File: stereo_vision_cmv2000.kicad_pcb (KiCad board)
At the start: 4 copper layers, 40 parts, among them P101 FI-RE51S-HF-R1500, U201 AP1084, U202 MCP1826S, U203 NCP1117ST20T3G, U401 CMV2000

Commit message: basic routing done
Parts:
- removed C218, C222, C228, C230, C407: 100n, SMD_Packages:SM0402_c
- removed TP401, TP402, TP403: TESTPOINT, Connect:TESTPOINT
- added C101: 100µ, SMD_Packages:SM1210, B.Cu at (117.7, 117.7)
- added C102: 100µ, SMD_Packages:SM1210, B.Cu at (117.7, 121.3)
- added C103: 100µ, SMD_Packages:SM1210, B.Cu at (117.7, 114.2)
- added C201: 100µ, SMD_Packages:SM1210, F.Cu at (154.1, 102.4)
- added C202: 100µ, SMD_Packages:SM1210, B.Cu at (147.6, 110.1)
- added C203: 330µ, Capacitors_SMD:c_elec_6.3x7.7, F.Cu at (153.4, 108.0)
- added C204: 33µ, SMD_Packages:SM0603_Capa, B.Cu at (147.3, 118.1)
- added C205: 10µ, SMD_Packages:SM0603_Capa, B.Cu at (148.1, 107.6)
- added C206: 10µ, SMD_Packages:SM0603_Capa, B.Cu at (147.3, 115.1)
- added C207: 330µ, Capacitors_SMD:c_elec_6.3x7.7, F.Cu at (153.4, 115.8)
- added C209: 10µ, SMD_Packages:SM0603_Capa, F.Cu at (153.8, 100.0)
- added C211: 330µ, Capacitors_SMD:c_elec_6.3x7.7, F.Cu at (153.4, 123.8)
- added C301: 4.7µ, SMD_Packages:SM0402_c, B.Cu at (138.2, 121.5)
- added C302: 100n, SMD_Packages:SM0402_c, B.Cu at (139.8, 116.5)
- added C306: 100n, SMD_Packages:SM0402_c, B.Cu at (131.8, 110.1)
- added C309: 4.7µ, SMD_Packages:SM0402_c, B.Cu at (121.5, 117.7)
- added C310: 4.7µ, SMD_Packages:SM0402_c, B.Cu at (139.8, 115.7)
- added C313: 4.7µ, SMD_Packages:SM0402_c, B.Cu at (129.6, 110.1)
- added C314: 4.7µ, SMD_Packages:SM0402_c, B.Cu at (121.5, 113.4)
- added C317: 4.7µ, SMD_Packages:SM0402_c, B.Cu at (131.1, 121.5)
- added C319: 4.7µ, SMD_Packages:SM0402_c, B.Cu at (121.5, 118.5)
- added C331: 100n, SMD_Packages:SM0402_c, B.Cu at (121.5, 116.2)
- added D201: LED, LEDs:LED-0603, F.Cu at (147.3, 103.0)
- added R201: 680, SMD_Packages:SM0603, F.Cu at (148.8, 103.0)
- added R302: R, SMD_Packages:SM0603, F.Cu at (139.3, 97.6)
- added R303: R, SMD_Packages:SM0603, F.Cu at (142.3, 97.6)
- added R304: 10k, SMD_Packages:SM0603, F.Cu at (143.8, 97.6)
- added R305: R, SMD_Packages:SM0603, F.Cu at (140.8, 97.6)
- added SYM: Symbol_OSHW-Logo_SilkScreen_07Jul2012, Symbols:Symbol_OSHW-Logo_SilkScreen, F.Cu at (112.3, 102.1)
- added TP301: TESTPOINT, Measurement_Points:Measurement_Point_Round-SMD-Pad_Small, F.Cu at (149.7, 129.3)
- added TP302: TESTPOINT, Measurement_Points:Measurement_Point_Round-SMD-Pad_Small, F.Cu at (151.8, 129.3)
- added TP303: TESTPOINT, Measurement_Points:Measurement_Point_Round-SMD-Pad_Small, F.Cu at (147.7, 129.3)
- added U401: MOUNTHOLE, owncomp:MOUNTING_HOLE, F.Cu at (110.8, 130.6)
- added U402: MOUNTHOLE, owncomp:MOUNTING_HOLE, F.Cu at (110.8, 95.6)
- added U403: MOUNTHOLE, owncomp:MOUNTING_HOLE, F.Cu at (155.8, 95.6)
- added U404: MOUNTHOLE, owncomp:MOUNTING_HOLE, F.Cu at (155.8, 130.6)
- added U405: MOUNTHOLE, owncomp:MOUNTING_HOLE, F.Cu at (142.8, 128.1)
- added U407: MOUNTHOLE, owncomp:MOUNTING_HOLE, F.Cu at (118.8, 104.1)
- added U408: MOUNTHOLE, owncomp:MOUNTING_HOLE, F.Cu at (118.8, 128.1)
- C208, C212: value 100n -> 33µ; footprint SMD_Packages:SM0402_c -> SMD_Packages:SM0603_Capa; moved to B.Cu
- C210: value 100n -> 10µ; footprint SMD_Packages:SM0402_c -> SMD_Packages:SM0603_Capa; moved to B.Cu
- C308: renamed from C214; moved to B.Cu
- C312: renamed from C217; moved to B.Cu
- C316: renamed from C221; moved to B.Cu
- C318: renamed from C224; moved to B.Cu
- C320: renamed from C226; moved to B.Cu
- C325: renamed from C401; moved to B.Cu
- C326: renamed from C402; moved to B.Cu
- C327: renamed from C403; moved to B.Cu
- C328: renamed from C404; moved to B.Cu
- C329: renamed from C405; moved to B.Cu
- C330: renamed from C406; moved to B.Cu
- C332: renamed from C408; moved to B.Cu
- C333: renamed from C409; moved to B.Cu
- C334: renamed from C410; moved to B.Cu
- C335: renamed from C411; moved to B.Cu
- C336: renamed from C412; moved to B.Cu
- C337: renamed from C413; moved to B.Cu
- C338: renamed from C414; moved to B.Cu
- C339: renamed from C415; moved to B.Cu
- C340: renamed from C416; moved to B.Cu
- C341: renamed from C417; moved to B.Cu
- C342: renamed from C418; moved to B.Cu
- C343: renamed from C419; moved to B.Cu
- P101: moved to B.Cu
- R301: renamed from R201; moved to B.Cu
- U201: value AP1084 -> 3.3V; moved to B.Cu
- U202: value MCP1826S -> 3.0V; moved to B.Cu
- U203: value NCP1117ST20T3G -> 2.0V; moved to B.Cu
- U301: renamed from U401; value CMV2000 -> CMV2000/4000
- moved C338 85.9 mm to (123.8, 121.5)
- moved U203 55.8 mm to (153.6, 123.8)
- moved U202 43.6 mm to (153.6, 115.8), turned to 90 degrees
- moved U201 41.8 mm to (154.1, 108.1), turned to 0 degrees
- moved C320 29.3 mm to (121.5, 119.3)
- moved C334 28.3 mm to (124.6, 121.5), turned to 90 degrees
- moved C336 28.1 mm to (125.3, 121.5), turned to 90 degrees
- moved C337 26.5 mm to (121.5, 114.9)
- moved C329 26.4 mm to (121.5, 112.6)
- moved C325 25.8 mm to (126.9, 121.5), turned to 90 degrees
- moved C312 25.8 mm to (121.5, 114.2)
- moved C308 25.7 mm to (121.5, 117.0)
- moved C326 24.1 mm to (126.9, 123.6), turned to 270 degrees
- moved C335 23.0 mm to (127.6, 121.5), turned to 90 degrees
- moved C343 23.0 mm to (126.1, 121.5), turned to 90 degrees
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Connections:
- net /OMV2000/LVDS_9_N renamed /CMV2000/LVDS_9_N
- net /OMV2000/LVDS_9_P renamed /CMV2000/LVDS_9_P
- net /OMV2000/SPI_CLK renamed /CMV2000/SPI_CLK
- net /OMV2000/SPI_IN renamed /CMV2000/SPI_IN
- net /OMV2000/SPI_OUT renamed /CMV2000/SPI_OUT
- C208 pad 1: GND -> /CMV2000/3.0V
- C208 pad 2: /OMV2000/3.3V -> GND
- C210 pad 1: GND -> /CMV2000/2.0V
- C210 pad 2: /OMV2000/2.0V -> GND
- C212 pad 1: GND -> /CMV2000/2.0V
- C212 pad 2: /OMV2000/2.0V -> GND
- C308 pad 2: /OMV2000/2.0V -> /CMV2000/2.0V
- C312 pad 2: /OMV2000/3.3V -> /CMV2000/3.3V
- C316 pad 2: /OMV2000/3.3V -> /CMV2000/3.3V
- C318 pad 2: /OMV2000/3.3V -> /CMV2000/3.3V
- C320 pad 2: /OMV2000/3.0V -> /CMV2000/3.0V
- C325 pad 1: /OMV2000/3.3V -> /CMV2000/3.3V
- C326 pad 1: /OMV2000/3.3V -> /CMV2000/3.3V
- C327 pad 1: /OMV2000/3.3V -> /CMV2000/3.3V
- C328 pad 1: /OMV2000/3.3V -> /CMV2000/3.3V
- P101 pad 1: /OMV2000/LVDS_1_N -> /CMV2000/LVDS_CLK_OUT_N
- P101 pad 10: /OMV2000/LVDS_5_P -> /CMV2000/LVDS_14_P
- P101 pad 11: /OMV2000/LVDS_6_P -> /CMV2000/LVDS_12_N
- P101 pad 12: /OMV2000/LVDS_6_N -> /CMV2000/LVDS_12_P
- P101 pad 13: /OMV2000/LVDS_7_N -> /CMV2000/LVDS_11_N
- P101 pad 14: /OMV2000/LVDS_7_P -> /CMV2000/LVDS_11_P
- P101 pad 15: /OMV2000/LVDS_8_N -> /CMV2000/LVDS_10_N
- P101 pad 16: /OMV2000/LVDS_8_P -> /CMV2000/LVDS_10_P
- P101 pad 19: /OMV2000/LVDS_10_N -> /CMV2000/LVDS_7_N
- P101 pad 2: /OMV2000/LVDS_1_P -> /CMV2000/LVDS_CLK_OUT_P
- P101 pad 20: /OMV2000/LVDS_10_P -> /CMV2000/LVDS_7_P
- P101 pad 21: /OMV2000/LVDS_11_N -> /CMV2000/LVDS_8_N
- P101 pad 22: /OMV2000/LVDS_11_P -> /CMV2000/LVDS_8_P
- P101 pad 23: /OMV2000/LVDS_12_N -> /CMV2000/LVDS_5_N
- P101 pad 24: /OMV2000/LVDS_12_P -> /CMV2000/LVDS_5_P
- P101 pad 25: /OMV2000/LVDS_13_N -> /CMV2000/LVDS_6_N
- P101 pad 26: /OMV2000/LVDS_13_P -> /CMV2000/LVDS_6_P
- P101 pad 27: /OMV2000/LVDS_14_P -> /CMV2000/LVDS_4_N
- P101 pad 28: /OMV2000/LVDS_14_N -> /CMV2000/LVDS_4_P
- P101 pad 29: /OMV2000/LVDS_15_N -> /CMV2000/LVDS_3_N
- P101 pad 3: /OMV2000/LVDS_2_N -> /CMV2000/LVDS_15_N
- P101 pad 30: /OMV2000/LVDS_15_P -> /CMV2000/LVDS_3_P
- P101 pad 31: /OMV2000/LVDS_16_N -> /CMV2000/LVDS_2_N
- P101 pad 32: /OMV2000/LVDS_16_P -> /CMV2000/LVDS_2_P
- P101 pad 33: /OMV2000/LVDS_CTR_N -> /CMV2000/LVDS_1_N
- P101 pad 34: /OMV2000/LVDS_CTR_P -> /CMV2000/LVDS_1_P
- P101 pad 35: /OMV2000/LVDS_CLK_OUT_N -> /CMV2000/LVDS_CTR_N
- P101 pad 36: /OMV2000/LVDS_CLK_OUT_P -> /CMV2000/LVDS_CTR_P
- P101 pad 37: Net-(P101-Pad37) -> /CMV2000/LVDS_CLK_IN_N
- P101 pad 38: /OMV2000/FRAME_REQ -> /CMV2000/LVDS_CLK_IN_P
- P101 pad 39: /OMV2000/T_EXP1 -> /CMV2000/FRAME_REQ
- P101 pad 4: /OMV2000/LVDS_2_P -> /CMV2000/LVDS_15_P
- P101 pad 40: /OMV2000/T_EXP2 -> /CMV2000/CLK_IN
- P101 pad 41: /OMV2000/SYS_RES_N -> /CMV2000/T_EXP2
- P101 pad 44: /OMV2000/SPI_EN -> /CMV2000/T_EXP1
- P101 pad 46: Net-(P101-Pad46) -> /CMV2000/SPI_EN
- P101 pad 47: Net-(P101-Pad47) -> /CMV2000/SYS_RES_N
- P101 pad 48: Net-(P101-Pad48) -> /Power Supply/5V
- P101 pad 49: Net-(P101-Pad49) -> /Power Supply/5V
- P101 pad 5: /OMV2000/LVDS_3_N -> /CMV2000/LVDS_16_N
- P101 pad 50: /OMV2000/LVDS_CLK_IN_N -> GND
- P101 pad 51: /OMV2000/LVDS_CLK_IN_P -> GND
- P101 pad 52: Net-(P101-Pad52) -> GND
- P101 pad 53: Net-(P101-Pad53) -> GND
- P101 pad 54: Net-(P101-Pad54) -> GND
- P101 pad 55: Net-(P101-Pad55) -> GND
- P101 pad 56: Net-(P101-Pad56) -> GND
- P101 pad 57: Net-(P101-Pad57) -> GND
- P101 pad 58: Net-(P101-Pad58) -> GND
- P101 pad 59: Net-(P101-Pad59) -> GND
- P101 pad 6: /OMV2000/LVDS_3_P -> /CMV2000/LVDS_16_P
- P101 pad 60: Net-(P101-Pad60) -> GND
- P101 pad 61: Net-(P101-Pad61) -> GND
- P101 pad 7: /OMV2000/LVDS_4_N -> /CMV2000/LVDS_13_N
- P101 pad 8: /OMV2000/LVDS_4_P -> /CMV2000/LVDS_13_P
- P101 pad 9: /OMV2000/LVDS_5_N -> /CMV2000/LVDS_14_N
- R301 pad 1: /OMV2000/LVDS_CLK_IN_N -> /CMV2000/LVDS_CLK_IN_N
- R301 pad 2: /OMV2000/LVDS_CLK_IN_P -> /CMV2000/LVDS_CLK_IN_P
- U201 pad 2: /OMV2000/3.3V -> /CMV2000/3.3V
- U202 pad 1: /OMV2000/3.3V -> /CMV2000/3.3V
- U202 pad 3: /OMV2000/3.0V -> /CMV2000/3.0V
- U203 pad 2: /OMV2000/2.0V -> /CMV2000/2.0V
- U203 pad 4: (no net) -> /CMV2000/2.0V
- U301 pad A10: /OMV2000/LVDS_15_N -> /CMV2000/LVDS_15_N
- U301 pad A11: /OMV2000/LVDS_15_P -> /CMV2000/LVDS_15_P
- U301 pad A2: /OMV2000/LVDS_2_N -> /CMV2000/LVDS_2_N
- U301 pad A3: /OMV2000/LVDS_2_P -> /CMV2000/LVDS_2_P
- U301 pad A4: /OMV2000/LVDS_5_N -> /CMV2000/LVDS_5_N
- U301 pad A5: /OMV2000/LVDS_5_P -> /CMV2000/LVDS_5_P
- U301 pad A7: /OMV2000/2.0V -> /CMV2000/2.0V
- U301 pad A8: /OMV2000/LVDS_12_N -> /CMV2000/LVDS_12_N
- U301 pad A9: /OMV2000/LVDS_12_P -> /CMV2000/LVDS_12_P
- U301 pad B1: /OMV2000/LVDS_CTR_N -> /CMV2000/LVDS_CTR_N
- U301 pad B10: /OMV2000/LVDS_13_P -> /CMV2000/LVDS_13_P
- U301 pad B11: /OMV2000/LVDS_CLK_OUT_N -> /CMV2000/LVDS_CLK_OUT_N
- U301 pad B12: /OMV2000/LVDS_CLK_OUT_P -> /CMV2000/LVDS_CLK_OUT_P
- U301 pad B2: /OMV2000/LVDS_CTR_P -> /CMV2000/LVDS_CTR_P
- U301 pad B3: /OMV2000/LVDS_4_N -> /CMV2000/LVDS_4_N
- U301 pad B4: /OMV2000/LVDS_4_P -> /CMV2000/LVDS_4_P
- U301 pad B5: /OMV2000/LVDS_7_N -> /CMV2000/LVDS_7_N
- U301 pad B6: /OMV2000/LVDS_7_P -> /CMV2000/LVDS_7_P
- U301 pad B7: /OMV2000/LVDS_10_N -> /CMV2000/LVDS_10_N
- U301 pad B8: /OMV2000/LVDS_10_P -> /CMV2000/LVDS_10_P
- U301 pad B9: /OMV2000/LVDS_13_N -> /CMV2000/LVDS_13_N
- U301 pad C10: /OMV2000/LVDS_16_N -> /CMV2000/LVDS_16_N
- U301 pad C11: /OMV2000/LVDS_16_P -> /CMV2000/LVDS_16_P
- U301 pad C2: /OMV2000/LVDS_1_N -> /CMV2000/LVDS_1_N
- U301 pad C3: /OMV2000/LVDS_1_P -> /CMV2000/LVDS_1_P
- U301 pad C4: /OMV2000/LVDS_6_N -> /CMV2000/LVDS_6_N
- U301 pad C5: /OMV2000/LVDS_6_P -> /CMV2000/LVDS_6_P
- U301 pad C7: /OMV2000/2.0V -> /CMV2000/2.0V
- U301 pad C8: /OMV2000/LVDS_11_N -> /CMV2000/LVDS_11_N
- U301 pad C9: /OMV2000/LVDS_11_P -> /CMV2000/LVDS_11_P
- U301 pad D1: /OMV2000/LVDS_CLK_IN_P -> /CMV2000/LVDS_CLK_IN_P
- U301 pad D10: /OMV2000/LVDS_14_P -> /CMV2000/LVDS_14_P
- U301 pad D2: /OMV2000/LVDS_CLK_IN_N -> /CMV2000/LVDS_CLK_IN_N
- U301 pad D3: /OMV2000/LVDS_3_N -> /CMV2000/LVDS_3_N
- U301 pad D4: /OMV2000/LVDS_3_P -> /CMV2000/LVDS_3_P
- U301 pad D5: /OMV2000/LVDS_8_N -> /CMV2000/LVDS_8_N
- U301 pad D6: /OMV2000/LVDS_8_P -> /CMV2000/LVDS_8_P
- U301 pad D9: /OMV2000/LVDS_14_N -> /CMV2000/LVDS_14_N
- U301 pad E1: /OMV2000/CLK_IN -> /CMV2000/CLK_IN
- U301 pad E2: /OMV2000/3.3V -> /CMV2000/3.3V
- U301 pad E4: /OMV2000/2.0V -> /CMV2000/2.0V
- U301 pad E6: /OMV2000/3.0V -> /CMV2000/3.0V
- U301 pad E7: /OMV2000/2.0V -> /CMV2000/2.0V
- U301 pad E8: /OMV2000/2.0V -> /CMV2000/2.0V
- U301 pad F2: /OMV2000/FRAME_REQ -> /CMV2000/FRAME_REQ
- U301 pad F7: /OMV2000/3.3V -> /CMV2000/3.3V
- U301 pad G1: /OMV2000/3.0V -> /CMV2000/3.0V
- U301 pad G12: /OMV2000/3.0V -> /CMV2000/3.0V
- U301 pad G3: /OMV2000/T_EXP2 -> /CMV2000/T_EXP2
- U301 pad G4: /OMV2000/SPI_EN -> /CMV2000/SPI_EN
- U301 pad H1: /OMV2000/3.3V -> /CMV2000/3.3V
- U301 pad H3: /OMV2000/T_EXP1 -> /CMV2000/T_EXP1
- U301 pad H5: /OMV2000/SYS_RES_N -> /CMV2000/SYS_RES_N
- U301 pad H6: /OMV2000/3.3V -> /CMV2000/3.3V
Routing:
- net /CMV2000/3.3V: track 0.00 -> 136.4 mm, vias 0 -> 25
- net /CMV2000/2.0V: track 0.00 -> 85.1 mm, vias 0 -> 18
- net (no net): track 0.00 -> 71.1 mm, vias 0 -> 54
- net GND: track 34.3 -> 105.4 mm, vias 0 -> 37
- net /CMV2000/3.0V: track 0.00 -> 58.7 mm, vias 0 -> 16
- net /Power Supply/5V: track 0.00 -> 51.8 mm, vias 0 -> 15
- net /OMV2000/3.3V: track 48.2 -> 0.00 mm, vias 12 -> 0
- net /CMV2000/SYS_RES_N: track 0.00 -> 37.0 mm, vias 0 -> 1
- net /CMV2000/SPI_EN: track 0.00 -> 31.2 mm, vias 0 -> 1
- net /CMV2000/T_EXP1: track 0.00 -> 31.0 mm, vias 0 -> 1
- net /CMV2000/SPI_CLK: track 1.91 -> 30.9 mm, vias 0 -> 1
- net /CMV2000/T_EXP2: track 0.00 -> 28.8 mm, vias 0 -> 1
- net /CMV2000/FRAME_REQ: track 0.00 -> 26.9 mm, vias 0 -> 1
- net /CMV2000/SPI_OUT: track 4.71 -> 31.6 mm, vias 0 -> 1
- net /CMV2000/SPI_IN: track 4.71 -> 29.3 mm, vias 0 -> 1
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- added copper zone on B.Cu, net /CMV2000/2.0V
- added copper zone on F.Cu, net /CMV2000/2.0V
- added copper zone on In1.Cu, net /CMV2000/2.0V
- added copper zone on B.Cu, net /CMV2000/3.0V
- added copper zone on F.Cu, net /CMV2000/3.0V
- added copper zone on B.Cu, net /CMV2000/3.3V
- added copper zone on F.Cu, net /CMV2000/3.3V
- added copper zone on In2.Cu, net /CMV2000/3.3V
- added copper zone on F.Cu, net /Power Supply/5V
- added copper zone on B.Cu, net GND
- added copper zone on F.Cu, net GND
- added copper zone on In1.Cu, net GND
- added copper zone on In2.Cu, net GND
- removed copper zone on In1.Cu, net /OMV2000/2.0V
- removed copper zone on B.Cu, net /OMV2000/3.0V
- removed copper zone on In2.Cu, net /OMV2000/3.3V
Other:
- board outline added: 50 x 40 mm
- net class Power_thick added: clearance 0.15, trace_width 2.54, via_dia 0.3, via_drill 0.25
- net class power_thin added: clearance 0.15, trace_width 1.27, via_dia 0.3, via_drill 0.25
- board text added: "10"
- board text added: "2.0V"
- board text added: "20"
- board text added: "2014 - xrpbot.org"
- board text added: "3.0V"
- board text added: "3.3V"
- board text added: "30"
- board text added: "40"
- board text added: "v1.0"

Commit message: v1.0
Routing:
- net GND: track 105.4 -> 127.1 mm

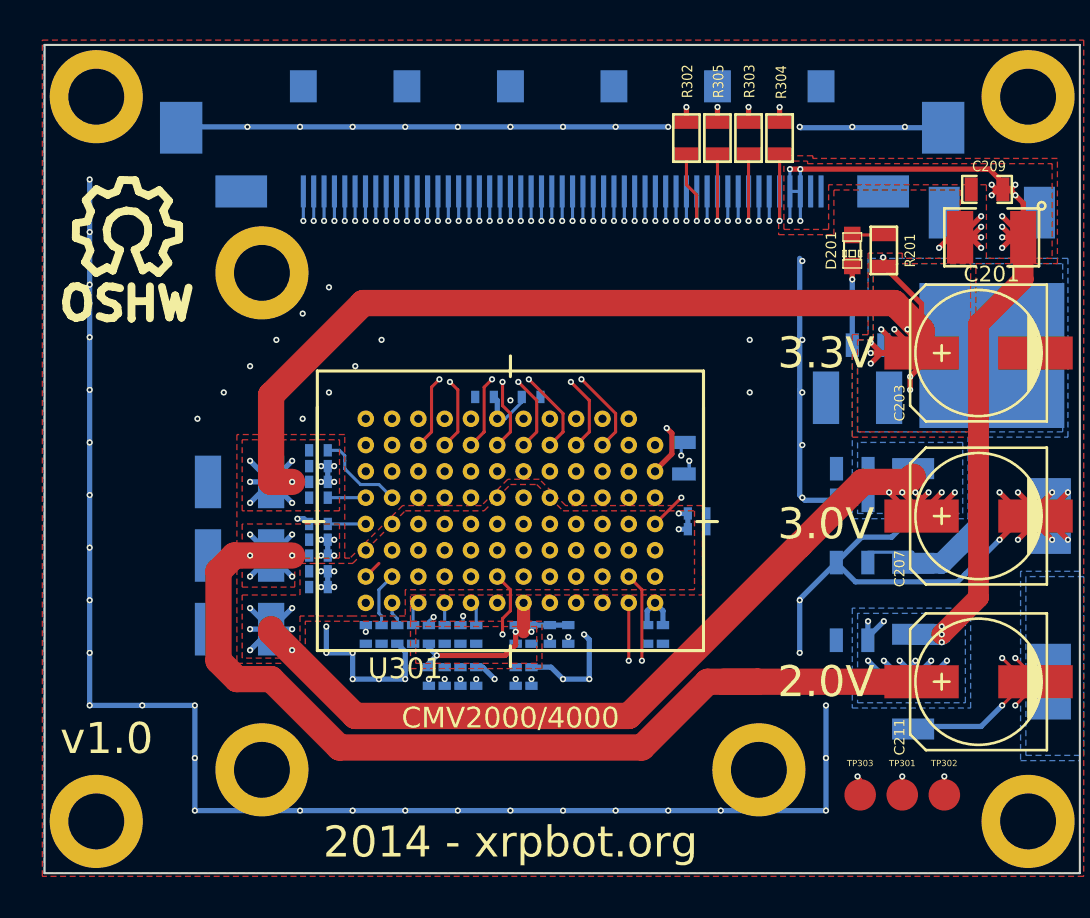
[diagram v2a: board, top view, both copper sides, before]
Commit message: fix some GND vias that were hanging in midair
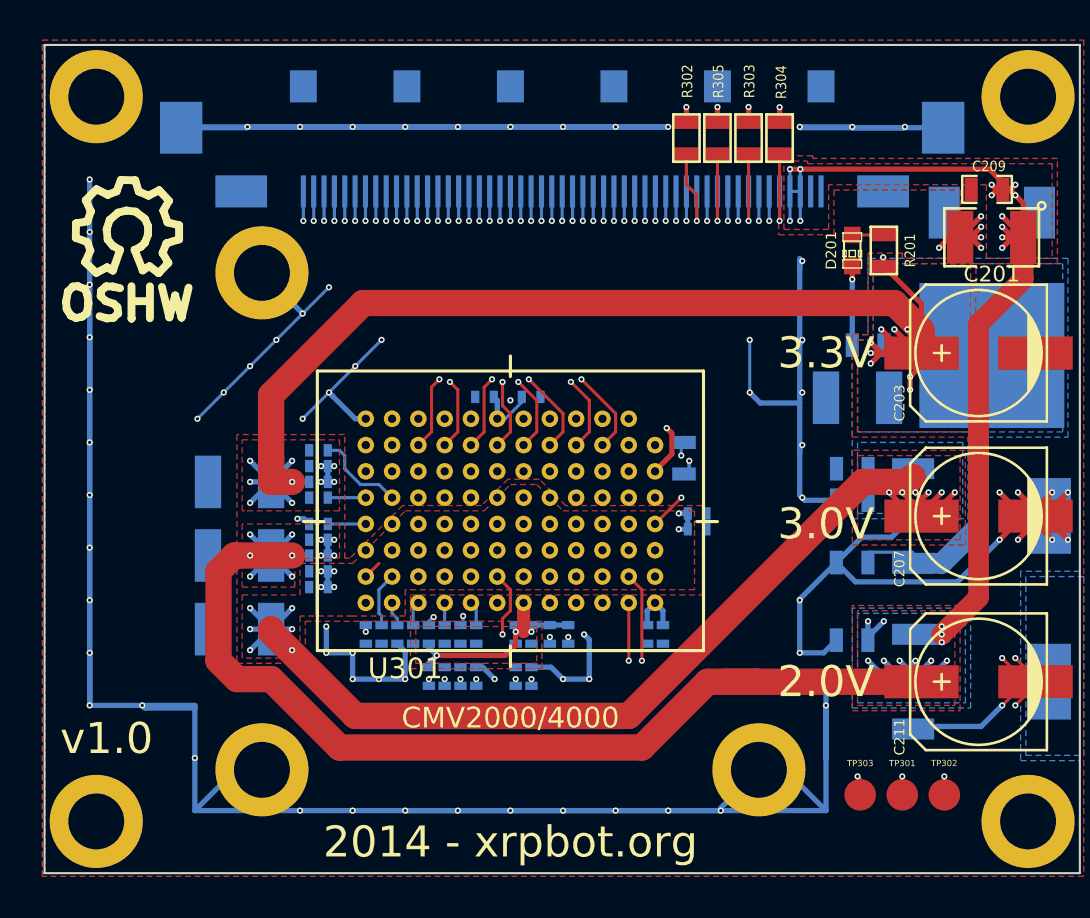
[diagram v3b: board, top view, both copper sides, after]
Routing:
- net GND: track 127.1 -> 326.1 mm, vias 37 -> 87
- net (no net): track 71.1 -> 0.00 mm, vias 54 -> 0

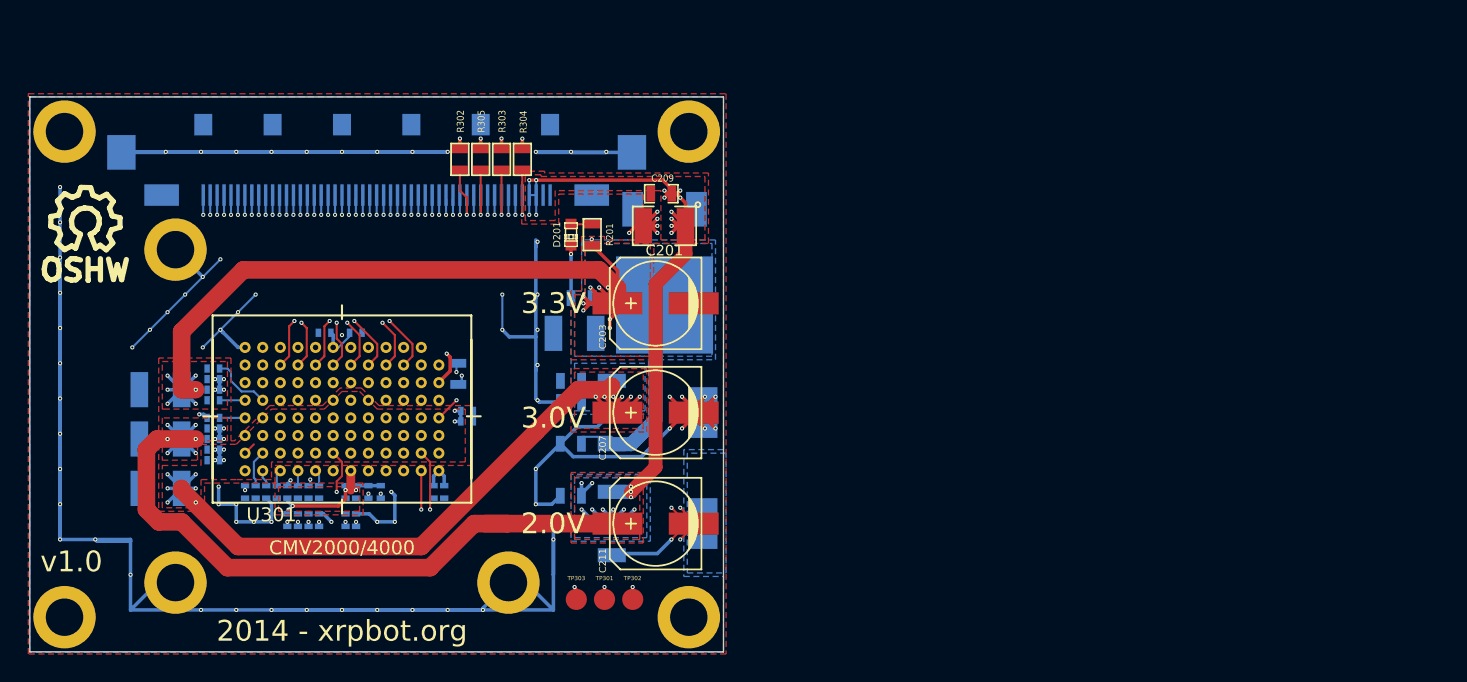
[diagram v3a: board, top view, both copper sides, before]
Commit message: change 0.5mm pitch to 0.3mm pitch connector and add proper ground between all LVDS pairs.
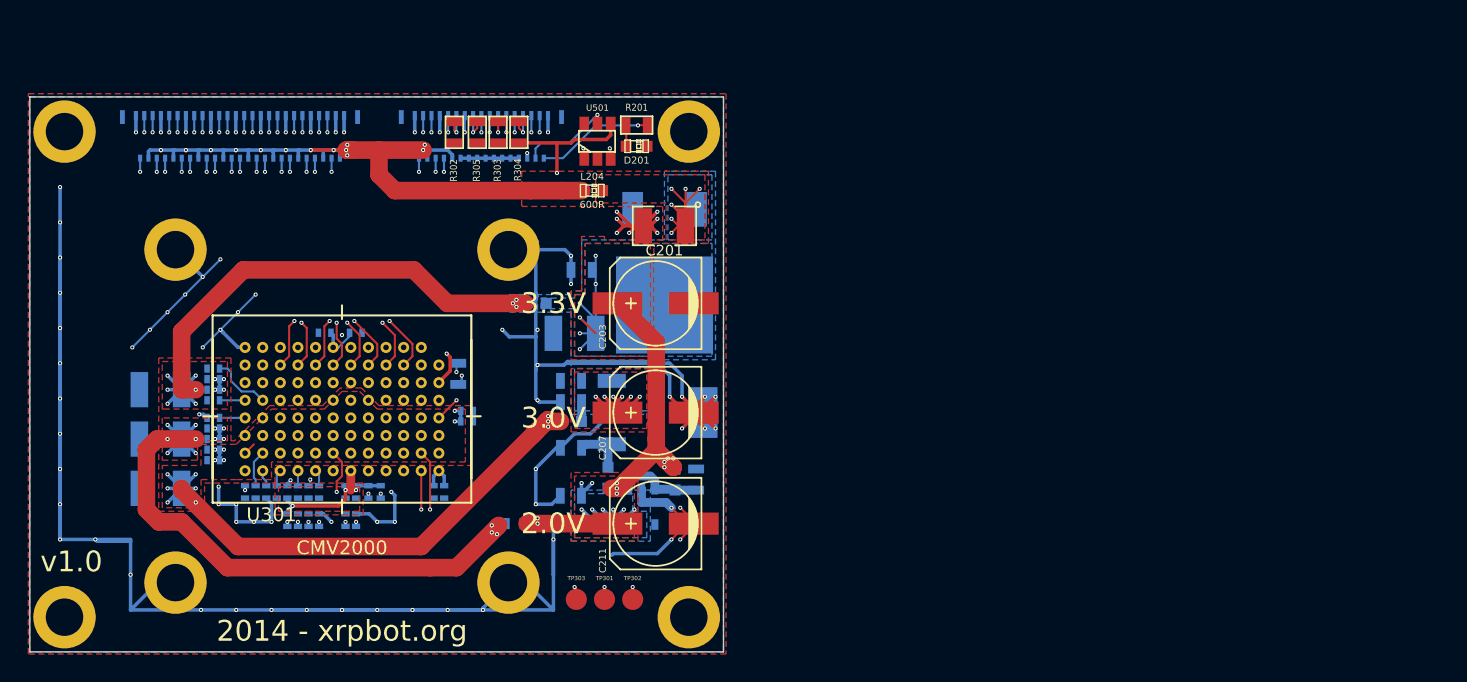
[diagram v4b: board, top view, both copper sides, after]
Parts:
- removed SYM: Symbol_OSHW-Logo_SilkScreen_07Jul2012, Symbols:Symbol_OSHW-Logo_SilkScreen
- added L201: 600R, LEDs:LED-0603, B.Cu at (143.3, 123.8)
- added L202: 600R, LEDs:LED-0603, B.Cu at (144.8, 108.0)
- added L203: 600R, LEDs:LED-0603, B.Cu at (147.3, 116.5)
- added L204: 600R, LEDs:LED-0603, F.Cu at (148.8, 99.8)
- added L205: 600R, LEDs:LED-0603, B.Cu at (154.8, 120.7)
- added L206: 600R, LEDs:LED-0603, B.Cu at (150.0, 120.5)
- added P102: CONN_33, owncomp:MOLEX_FPC_0.3mm_33pin, B.Cu at (140.9, 94.4)
- added U406: MOUNTHOLE, owncomp:MOUNTING_HOLE, F.Cu at (142.5, 103.7)
- added U501: 24AA025E48, SMD_Packages:SOT23_6, F.Cu at (149.2, 96.3)
- C209: value 10µ -> 1µ; moved to B.Cu
- C210: value 10µ -> 1µ
- P101: value FI-RE51S-HF-R1500 -> CONN_51; footprint owncomp:FI-RE51S-HF-R1500 -> owncomp:MOLEX_FPC_0.3mm_51pin
- U201: value 3.3V -> AP1084
- U202: value 3.0V -> MCP1826S
- U203: value 2.0V -> RT9017-20GBR; footprint SMD_Packages:SOT223 -> SMD_Packages:SOT23-5
- U301: value CMV2000/4000 -> CMV2000
- moved C209 20.8 mm to (156.3, 120.7), turned to 90 degrees
- moved C204 12.6 mm to (148.1, 105.5)
- moved P101 11.1 mm to (123.5, 94.4)
- moved C205 10.8 mm to (147.3, 118.4)
- moved R201 8.52 mm to (152.0, 95.1), turned to 0 degrees
- moved D201 7.94 mm to (152.0, 96.6), turned to 0 degrees
- moved R302 1.99 mm to (138.9, 95.6), turned to 270 degrees
- moved R303 1.97 mm to (142.1, 95.6), turned to 270 degrees
- moved R304 1.97 mm to (143.6, 95.6), turned to 90 degrees
- moved R305 1.97 mm to (140.6, 95.6), turned to 270 degrees
- moved U203 1.66 mm to (152.4, 122.6), turned to 0 degrees
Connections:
- C201 pad 1: /Power Supply/5V -> Net-(C201-Pad1)
- C202 pad 1: /CMV2000/3.3V -> Net-(C202-Pad1)
- C203 pad 1: /CMV2000/3.3V -> Net-(C202-Pad1)
- C204 pad 1: /CMV2000/3.3V -> Net-(C202-Pad1)
- C205 pad 1: /CMV2000/3.3V -> Net-(C205-Pad1)
- C206 pad 1: /CMV2000/3.0V -> Net-(C206-Pad1)
- C207 pad 1: /CMV2000/3.0V -> Net-(C206-Pad1)
- C208 pad 1: /CMV2000/3.0V -> Net-(C206-Pad1)
- C209 pad 1: /Power Supply/5V -> Net-(C209-Pad1)
- C210 pad 1: /CMV2000/2.0V -> Net-(C210-Pad1)
- C211 pad 1: /CMV2000/2.0V -> Net-(C210-Pad1)
- C212 pad 1: /CMV2000/2.0V -> Net-(C210-Pad1)
- P101 pad 1: /CMV2000/LVDS_CLK_OUT_N -> GND
- P101 pad 10: /CMV2000/LVDS_14_P -> /Power Supply/5V
- P101 pad 11: /CMV2000/LVDS_12_N -> /CMV2000/LVDS_13_N
- P101 pad 12: /CMV2000/LVDS_12_P -> /CMV2000/LVDS_13_P
- P101 pad 13: /CMV2000/LVDS_11_N -> GND
- P101 pad 14: /CMV2000/LVDS_11_P -> /CMV2000/LVDS_14_N
- P101 pad 15: /CMV2000/LVDS_10_N -> /CMV2000/LVDS_14_P
- P101 pad 16: /CMV2000/LVDS_10_P -> /Power Supply/5V
- P101 pad 17: /CMV2000/LVDS_9_N -> /CMV2000/LVDS_12_N
- P101 pad 18: /CMV2000/LVDS_9_P -> /CMV2000/LVDS_12_P
- P101 pad 19: /CMV2000/LVDS_7_N -> GND
- P101 pad 2: /CMV2000/LVDS_CLK_OUT_P -> /CMV2000/LVDS_CLK_OUT_N
- P101 pad 20: /CMV2000/LVDS_7_P -> /CMV2000/LVDS_11_N
- P101 pad 21: /CMV2000/LVDS_8_N -> /CMV2000/LVDS_11_P
- P101 pad 22: /CMV2000/LVDS_8_P -> /Power Supply/5V
- P101 pad 23: /CMV2000/LVDS_5_N -> /CMV2000/LVDS_10_N
- P101 pad 24: /CMV2000/LVDS_5_P -> /CMV2000/LVDS_10_P
- P101 pad 25: /CMV2000/LVDS_6_N -> GND
- P101 pad 26: /CMV2000/LVDS_6_P -> /CMV2000/LVDS_9_N
- P101 pad 27: /CMV2000/LVDS_4_N -> /CMV2000/LVDS_9_P
- P101 pad 28: /CMV2000/LVDS_4_P -> /Power Supply/5V
- P101 pad 29: /CMV2000/LVDS_3_N -> /CMV2000/LVDS_7_N
- P101 pad 3: /CMV2000/LVDS_15_N -> /CMV2000/LVDS_CLK_OUT_P
- P101 pad 30: /CMV2000/LVDS_3_P -> /CMV2000/LVDS_7_P
- P101 pad 31: /CMV2000/LVDS_2_N -> GND
- P101 pad 32: /CMV2000/LVDS_2_P -> /CMV2000/LVDS_8_N
- P101 pad 33: /CMV2000/LVDS_1_N -> /CMV2000/LVDS_8_P
- P101 pad 34: /CMV2000/LVDS_1_P -> /Power Supply/5V
- P101 pad 35: /CMV2000/LVDS_CTR_N -> /CMV2000/LVDS_5_N
- P101 pad 36: /CMV2000/LVDS_CTR_P -> /CMV2000/LVDS_5_P
- P101 pad 37: /CMV2000/LVDS_CLK_IN_N -> GND
- P101 pad 38: /CMV2000/LVDS_CLK_IN_P -> /CMV2000/LVDS_6_N
- P101 pad 39: /CMV2000/FRAME_REQ -> /CMV2000/LVDS_6_P
- P101 pad 4: /CMV2000/LVDS_15_P -> /Power Supply/5V
- P101 pad 40: /CMV2000/CLK_IN -> /Power Supply/5V
- P101 pad 41: /CMV2000/T_EXP2 -> /CMV2000/LVDS_4_N
- P101 pad 42: /CMV2000/SPI_IN -> /CMV2000/LVDS_4_P
- P101 pad 43: /CMV2000/SPI_OUT -> GND
- P101 pad 44: /CMV2000/T_EXP1 -> /CMV2000/LVDS_3_N
- P101 pad 45: /CMV2000/SPI_CLK -> /CMV2000/LVDS_3_P
- P101 pad 46: /CMV2000/SPI_EN -> /Power Supply/5V
- P101 pad 47: /CMV2000/SYS_RES_N -> /CMV2000/LVDS_2_N
- P101 pad 48: /Power Supply/5V -> /CMV2000/LVDS_2_P
- P101 pad 49: /Power Supply/5V -> GND
- P101 pad 5: /CMV2000/LVDS_16_N -> /CMV2000/LVDS_15_N
- P101 pad 50: GND -> /Power Supply/5V
- P101 pad 52: GND -> (no net)
- P101 pad 53: GND -> (no net)
- P101 pad 6: /CMV2000/LVDS_16_P -> /CMV2000/LVDS_15_P
- P101 pad 7: /CMV2000/LVDS_13_N -> GND
- P101 pad 8: /CMV2000/LVDS_13_P -> /CMV2000/LVDS_16_N
- P101 pad 9: /CMV2000/LVDS_14_N -> /CMV2000/LVDS_16_P
- R201 pad 2: /CMV2000/3.3V -> /Power Supply/LED_3.3V
- U201 pad 2: /CMV2000/3.3V -> Net-(C202-Pad1)
- U201 pad 3: /Power Supply/5V -> Net-(C201-Pad1)
- U202 pad 1: /CMV2000/3.3V -> Net-(C205-Pad1)
- U202 pad 3: /CMV2000/3.0V -> Net-(C206-Pad1)
- U203 pad 1: GND -> Net-(C209-Pad1)
- U203 pad 2: /CMV2000/2.0V -> GND
- U203 pad 3: /Power Supply/5V -> Net-(C209-Pad1)
- U203 pad 4: /CMV2000/2.0V -> Net-(U203-Pad4)
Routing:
- net Net-(C202-Pad1): track 0.00 -> 51.1 mm, vias 0 -> 13
- net Net-(C210-Pad1): track 0.00 -> 29.3 mm, vias 0 -> 10
- net /CMV2000/3.3V: track 136.4 -> 107.3 mm, vias 25 -> 19
- net GND: track 326.1 -> 304.0 mm, vias 87 -> 84
- net /CMV2000/2.0V: track 85.1 -> 66.2 mm, vias 18 -> 13
- net Net-(C206-Pad1): track 0.00 -> 11.8 mm, vias 0 -> 6
- net Net-(C201-Pad1): track 0.00 -> 11.6 mm, vias 0 -> 6
- net /CMV2000/LVDS_15_N: track 12.6 -> 23.0 mm
- net /CMV2000/LVDS_CLK_OUT_P: track 14.6 -> 24.1 mm
- net /CMV2000/3.0V: track 58.7 -> 49.6 mm, vias 16 -> 13
- net /CMV2000/LVDS_4_N: track 13.1 -> 21.9 mm
- net /CMV2000/LVDS_16_P: track 15.6 -> 24.3 mm
- net /CMV2000/LVDS_13_N: track 14.1 -> 22.7 mm
- net /CMV2000/LVDS_5_N: track 11.6 -> 20.1 mm
- net /CMV2000/LVDS_6_P: track 13.5 -> 22.0 mm
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- added copper zone on B.Cu, net Net-(C201-Pad1)
- added copper zone on F.Cu, net Net-(C201-Pad1)
- added copper zone on B.Cu, net Net-(C202-Pad1)
- added copper zone on F.Cu, net Net-(C202-Pad1)
- added copper zone on B.Cu, net Net-(C206-Pad1)
- added copper zone on F.Cu, net Net-(C206-Pad1)
- added copper zone on B.Cu, net Net-(C210-Pad1)
- removed copper zone on B.Cu, net /CMV2000/2.0V
- removed copper zone on B.Cu, net /CMV2000/3.0V
- removed copper zone on F.Cu, net /Power Supply/5V
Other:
- board text removed: "10"
- board text removed: "20"
- board text removed: "30"
- board text removed: "40"
